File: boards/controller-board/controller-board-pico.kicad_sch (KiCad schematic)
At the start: 62 parts, among them J1 Phoenix 1935161, J2 Conn_01x02, J3 Conn_01x02, J4 Conn_01x02, J5 Conn_01x03, J6 Phoenix 1995499, J7 Conn_01x03, J8 Conn_01x03, Q1 PMV45EN, Q2 Goford_G11S_20V_11A, U2 ADS1015IRUGR, U4 RPi_Pico, U5 MCP4728

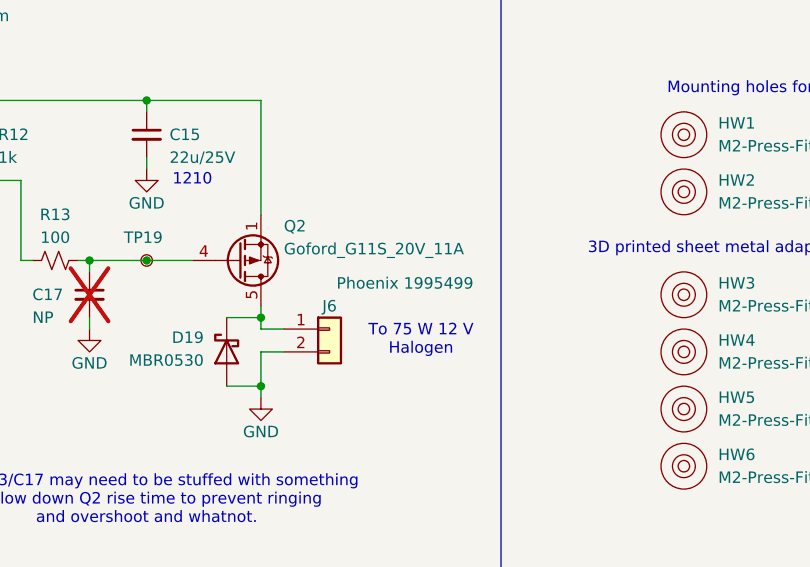
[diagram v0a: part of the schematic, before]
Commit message: Updates to sch and brd after fab. Fixed J6 part number, updated EOL parts to newer part numbers.
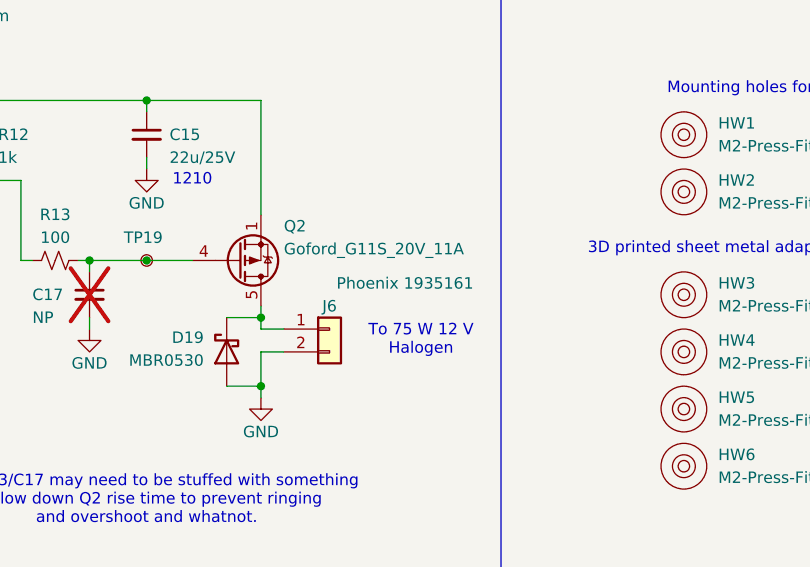
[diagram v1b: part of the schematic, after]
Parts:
- D19: DPN MBR0530CT-ND -> MBR0530T3GOSCT-ND; MPN MBR0530 -> MBR0530T3G
- J6: value Phoenix 1995499 -> Phoenix 1935161; DPN 277-6718-ND -> 277-1667-ND; MPN 1995499 -> 1935161
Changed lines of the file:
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@@
 			)
 		)
-		(property "Value" "Phoenix 1995499"
+		(property "Value" "Phoenix 1935161"
 			(at 363.982 85.09 0)
 			(effects
@@
 			)
 		)
-		(property "Description" "2 Position Terminal Block Header, Male Pins, Shrouded (4 Side) 0.138\" (3.50mm) 90°, Right Angle Through Hole"
+		(property "Description" "2 Position Wire to Board Terminal Block Horizontal with Board 0.197\" (5.00mm) Through Hole"
 			(at 355.6 90.17 0)
 			(effects
@@
 			)
 		)
-		(property "DPN" "277-6718-ND"
+		(property "DPN" "277-1667-ND"
 			(at 355.6 90.17 0)
 			(effects
@@
 			)
 		)
-		(property "MPN" "1995499"
+		(property "MPN" "1935161"
 			(at 355.6 90.17 0)
 			(effects
@@
 			)
 		)
-		(property "Description" "30V 0.5A Schottky Power Rectifier Diode, SOD-123"
+		(property "Description" "Diode 30 V 500mA Surface Mount SOD-123"
 			(at 344.17 92.71 0)
 			(effects
@@
 			)
 		)
-		(property "DPN" "MBR0530CT-ND"
+		(property "DPN" "MBR0530T3GOSCT-ND"
 			(at 344.17 92.71 0)
 			(effects
@@
 			)
 		)
-		(property "MPN" "MBR0530"
+		(property "MPN" "MBR0530T3G"
 			(at 344.17 92.71 0)
 			(effects
